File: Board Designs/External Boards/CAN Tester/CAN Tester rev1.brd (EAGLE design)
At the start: 160 x 100 mm, 25 parts, among them M1 Minifit, M2 Nanofit, U1 ISOLATED CAN TERMINAL, U2 TERMINATION_RESISTOR_JUMPER, U3 TEENSY_3.2_SIMPLE, U4 CHARACTER_LCD

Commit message: Moved the location of the can tester folder.
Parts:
- U1: value ISOLATED CAN TERMINAL -> ISOLATED CAN TRANSCIEVER
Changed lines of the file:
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@@
 <elements>
 <element name="U3" library="HyTechDevices" package="TEENSY_3.2_SIMPLE" value="TEENSY_3.2_SIMPLE" x="-19.05" y="1.27"/>
-<element name="U1" library="HyTechDevices" package="DUB8" value="ISOLATED CAN TERMINAL" x="-30.48" y="-30.48"/>
+<element name="U1" library="HyTechDevices" package="DUB8" value="ISOLATED CAN TRANSCIEVER" x="-30.48" y="-30.48"/>
 <element name="INCOMING" library="HyTechDevices" package="LED-805" value="YELLOW" x="-64.77" y="-72.39"/>
 <element name="OUTGOING" library="HyTechDevices" package="LED-805" value="BLUE" x="-71.12" y="-72.39"/>

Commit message: Verified schematic, but had to restart board
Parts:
- moved C2 306.9 mm to (-19.1, 116.8)
- moved C1 305.6 mm to (-15.2, 116.8)
- moved 5V_REGULATOR 282.7 mm to (-17.8, 110.5)
- moved CONTRAST_POT 257.5 mm to (-38.1, 81.3)
- moved R5 229.8 mm to (-38.1, 116.8)
- moved R4 228.3 mm to (-34.3, 116.8)
- moved R3 226.8 mm to (-30.5, 116.8)
- moved R2 225.4 mm to (-26.7, 116.8)
- moved R1 224.1 mm to (-22.9, 116.8)
- moved R_SPARE_BUTTON 219.9 mm to (-81.3, 108.0)
- moved R_MODE_SWITCH 217.2 mm to (-86.4, 108.0)
- moved M1 203.4 mm to (-63.5, 77.5)
- moved CAN_TERMINATION_RESISTOR 202.6 mm to (-74.9, 108.0)
- moved U4 200.9 mm to (-94.0, 39.4)
- moved U2 200.8 mm to (-67.3, 108.0)
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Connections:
- removed net N$15: R_MODE_SWITCH.2
- net GND: now also R_MODE_SWITCH.2

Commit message: Finished CAN_Tester Board
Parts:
- moved R_MODE_SWITCH 164.9 mm to (77.5, 88.9), turned to 270 degrees
- moved R_SPARE_BUTTON 160.8 mm to (77.5, 82.5), turned to 90 degrees
- moved CAN_TERMINATION_RESISTOR 153.8 mm to (67.3, 49.5), turned to 90 degrees
- moved INCOMING 153.6 mm to (72.4, 58.4), turned to 270 degrees
- moved U2 148.3 mm to (67.3, 45.7), turned to 90 degrees
- moved M1 147.3 mm to (64.8, 5.08)
- moved OUTGOING 146.7 mm to (72.4, 63.5), turned to 270 degrees
- moved SPARE 135.3 mm to (72.4, 78.7), turned to 270 degrees
- moved SPARE_BUTTON 124.5 mm to (71.1, 83.8)
- moved M2 123.4 mm to (48.3, 14.0)
- moved R5 113.3 mm to (68.6, 78.7), turned to 180 degrees
- moved MODE_SWITCH 113.0 mm to (71.1, 92.7)
- moved R4 111.6 mm to (68.6, 73.7), turned to 180 degrees
- moved ACKERR 111.3 mm to (72.4, 68.6), turned to 270 degrees
- moved R3 110.2 mm to (68.6, 68.6), turned to 180 degrees
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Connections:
- removed net VSS: U4.1
- net GND: now also U4.1
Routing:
- net GND: track 0.00 -> 309.8 mm
- net +5V: track 0.00 -> 139.2 mm
- net +3V3: track 0.00 -> 101.9 mm
- net CANL: track 0.00 -> 92.8 mm
- net +12V: track 0.00 -> 77.4 mm
- net CANH: track 0.00 -> 77.2 mm
- net CANTX: track 0.00 -> 42.6 mm
- net CANRX: track 0.00 -> 39.6 mm
- net N$22: track 0.00 -> 38.3 mm
- net N$20: track 0.00 -> 28.7 mm
- net VO: track 0.00 -> 27.4 mm
- net N$19: track 0.00 -> 26.8 mm
- net N$21: track 0.00 -> 26.3 mm
- net N$13: track 0.00 -> 17.5 mm
- net N$18: track 0.00 -> 17.4 mm
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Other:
- board size 160 x 100 mm -> 83.8 x 100.3 mm

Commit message: Actually finished CAN Tester board. Ready to be made for rev1
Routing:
- net GND: track 309.8 -> 326.9 mm
- net +12V: track 77.4 -> 79.2 mm

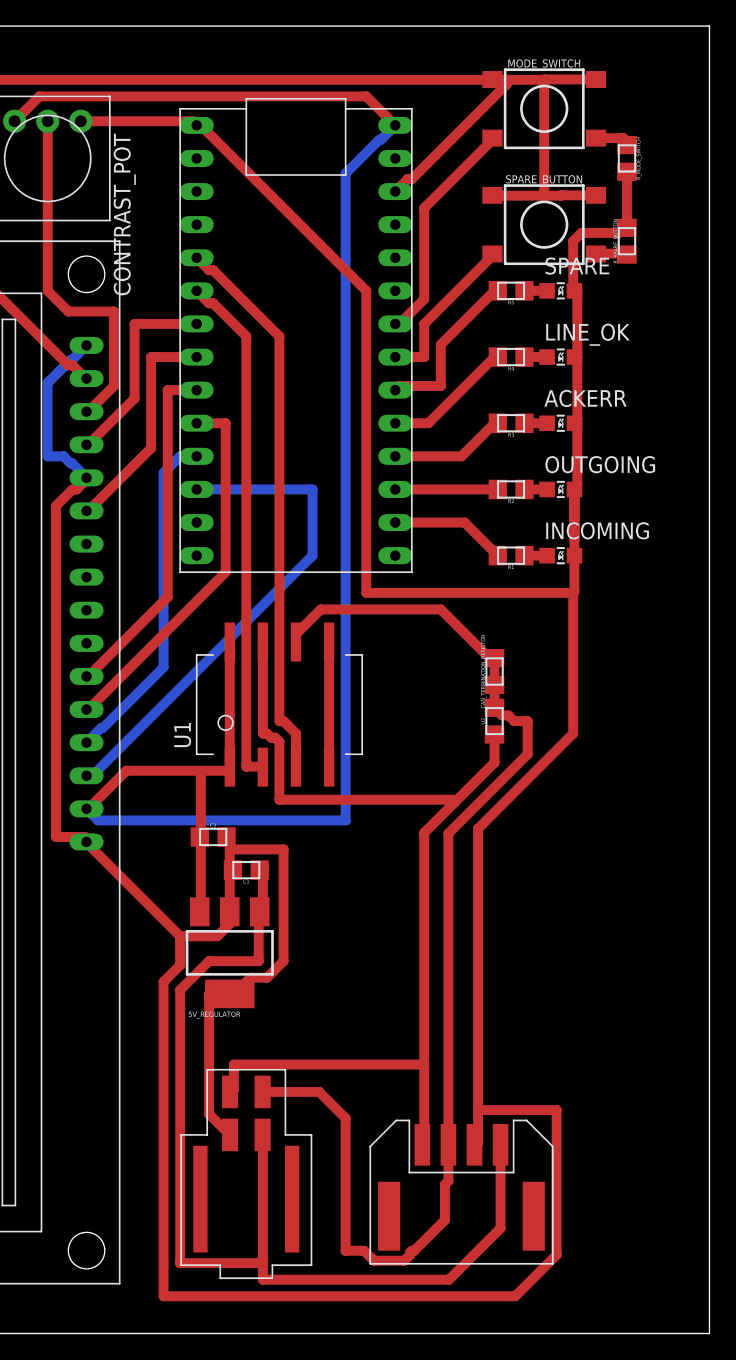
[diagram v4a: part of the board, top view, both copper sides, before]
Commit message: Added anothe rminifit and nano fit. Changed some components to through hole.
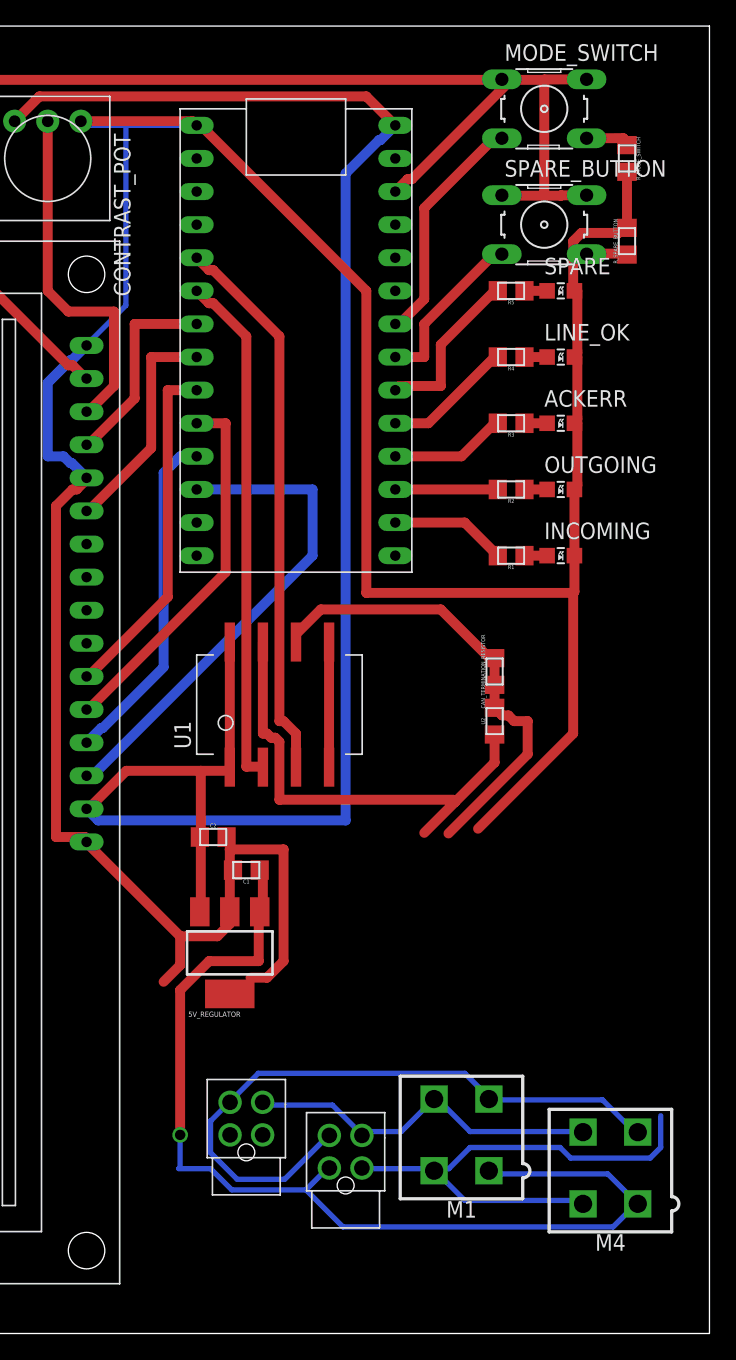
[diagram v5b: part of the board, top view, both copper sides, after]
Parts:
- added M3: Nanofit-1, HyTechDevices:NANO-FIT_VERTICAL-4
- added M4: Minifit-1, HyTechDevices:MINIFIT_5566-4
- M1: device HyTechDevices:DURACLIK_RIGHT_ANGLE-4 -> HyTechDevices:MINIFIT_5566-4
- M2: device HyTechDevices:NANO-FIT_RIGHT_ANGLE-4-SURFACE -> HyTechDevices:NANO-FIT_VERTICAL-4
- MODE_SWITCH, SPARE_BUTTON: device HyTechDevices:TACTILE_SWITCH_SMD_6.2MM_TALL -> HyTechDevices:B3F-10XX
- moved M1 8.89 mm to (64.8, 14.0)
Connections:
- net +12V: now also M2.P$1, M3.P$1, M4.1; no longer M2.1
- net +3V3: now also MODE_SWITCH.1, MODE_SWITCH.2, SPARE_BUTTON.1, SPARE_BUTTON.2; no longer MODE_SWITCH.B1, MODE_SWITCH.B2, SPARE_BUTTON.B1, SPARE_BUTTON.B2
- net CANH: now also M2.P$4, M3.P$4, M4.4; no longer M2.4
- net CANL: now also M2.P$3, M3.P$3, M4.3; no longer M2.3
- net GND: now also M2.P$2, M3.P$2, M4.2; no longer M2.2
- net N$12: now also MODE_SWITCH.4; no longer MODE_SWITCH.A2
- net N$13: now also MODE_SWITCH.3; no longer MODE_SWITCH.A1
- net N$14: now also SPARE_BUTTON.4; no longer SPARE_BUTTON.A2
- net N$3: now also SPARE_BUTTON.3; no longer SPARE_BUTTON.A1
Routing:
- net GND: track 326.9 -> 277.9 mm
- net CANH: track 77.2 -> 64.3 mm
- net CANL: track 92.6 -> 86.1 mm
- net +12V: track 79.2 -> 81.0 mm, vias 0 -> 1
- net N$14: track 2.46 -> 3.18 mm
- net N$12: track 2.74 -> 3.46 mm
- net N$3: track 12.3 -> 12.9 mm
- net N$13: track 17.5 -> 18.1 mm

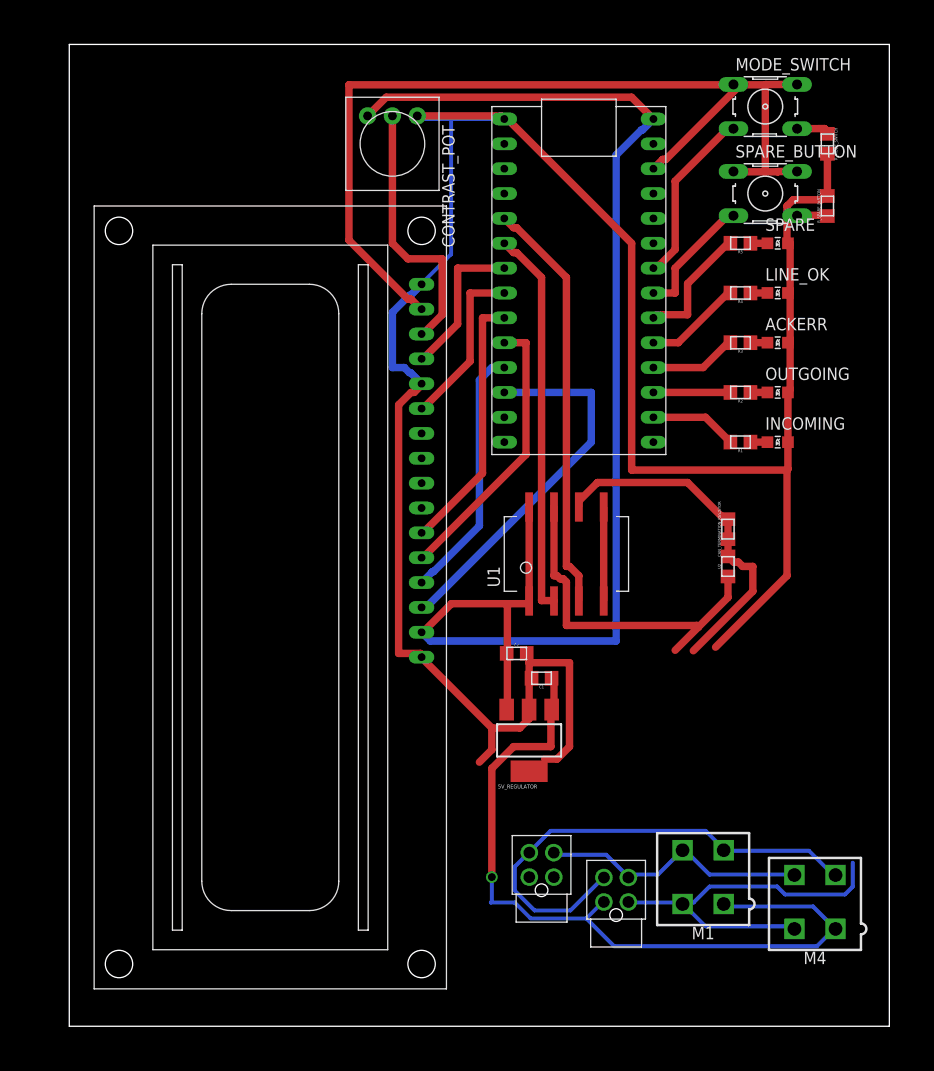
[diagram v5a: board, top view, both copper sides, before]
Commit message: Working on changes so the board can be made in the electronics lab
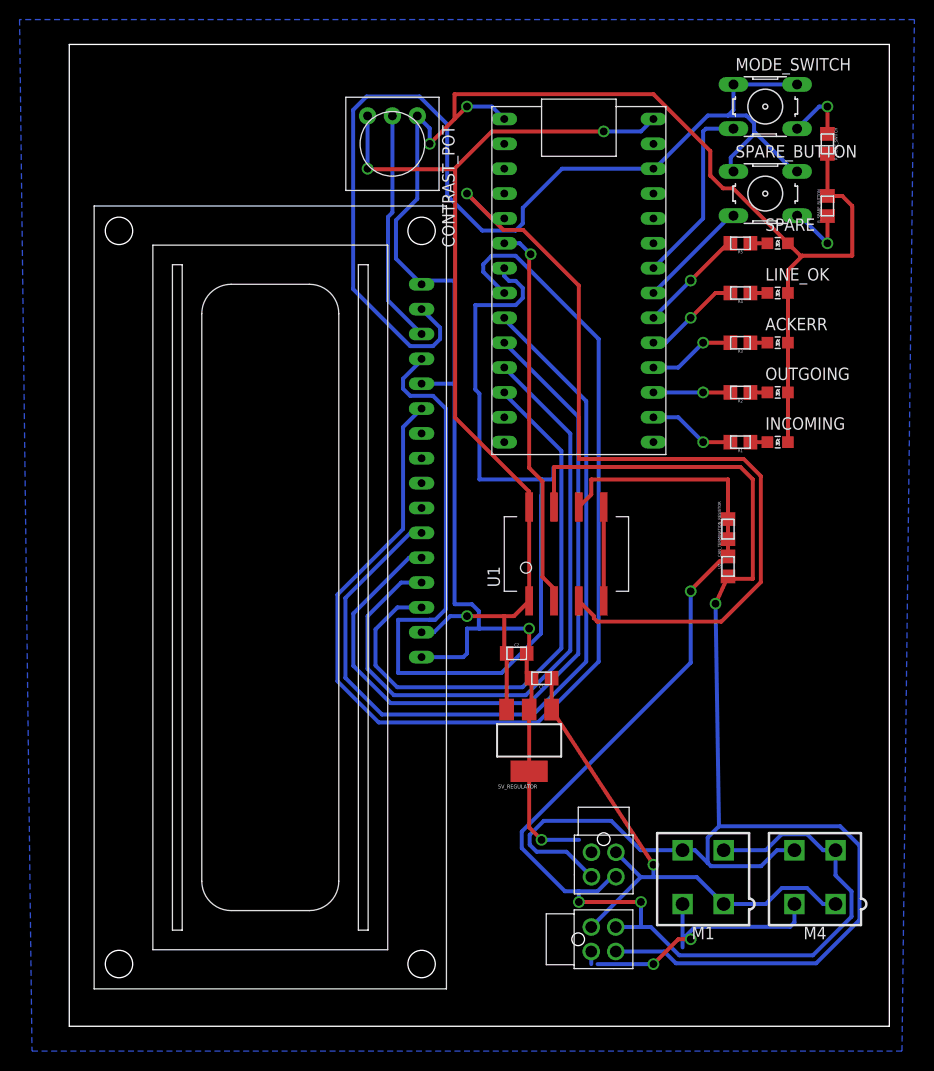
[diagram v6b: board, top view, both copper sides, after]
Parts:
- moved M2 8.13 mm to (53.3, 7.62), turned to 270 degrees
- moved M3 5.24 mm to (54.6, 16.5), turned to 180 degrees
- moved M4 2.54 mm to (76.2, 14.0)
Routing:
- net N$18: track 17.4 -> 114.9 mm
- net N$17: track 15.6 -> 108.9 mm
- net CANH: track 64.3 -> 156.7 mm, vias 0 -> 1
- net N$19: track 26.8 -> 85.7 mm
- net N$20: track 28.7 -> 76.3 mm
- net GND: track 277.9 -> 230.7 mm, vias 0 -> 6
- net CANL: track 86.1 -> 133.2 mm, vias 0 -> 3
- net CANTX: track 42.6 -> 89.3 mm, vias 0 -> 1
- net N$21: track 26.3 -> 67.8 mm
- net +5V: track 139.2 -> 106.1 mm, vias 0 -> 3
- net +12V: track 81.0 -> 56.6 mm
- net N$22: track 38.3 -> 60.6 mm
- net +3V3: track 102.1 -> 113.4 mm
- net N$14: track 3.18 -> 7.05 mm, vias 0 -> 1
- net VO: track 27.4 -> 23.9 mm
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- added copper zone on layer 16, net GND

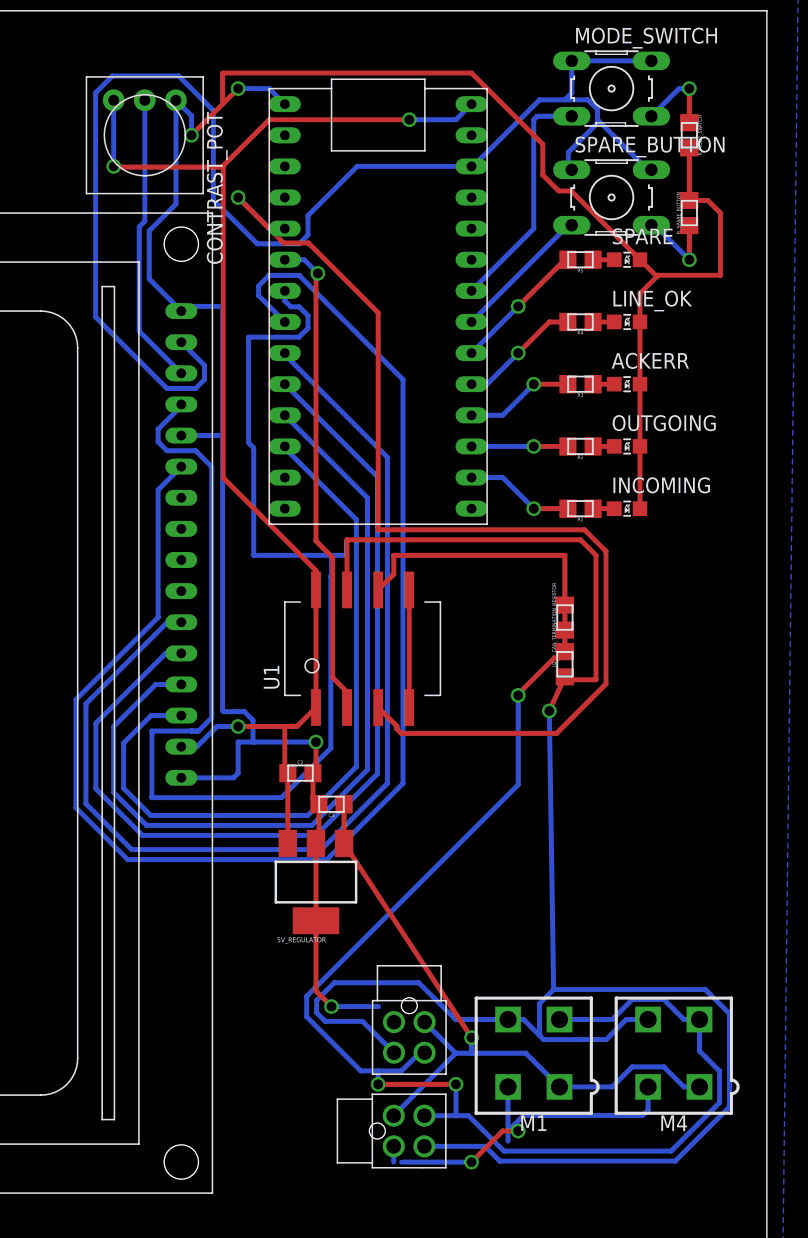
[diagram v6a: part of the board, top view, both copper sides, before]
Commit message: Almost done with CAN tester board, just changed the jumper package
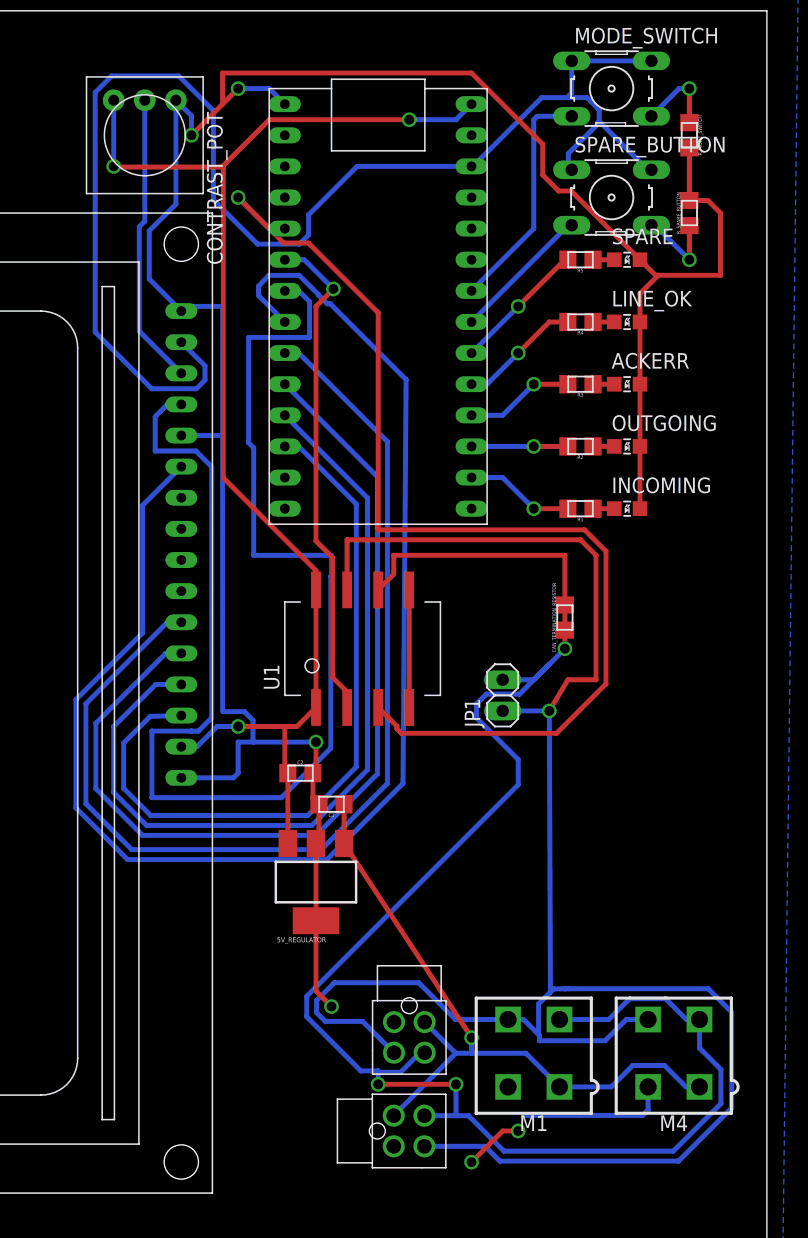
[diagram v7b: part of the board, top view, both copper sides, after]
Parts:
- removed U2: TERMINATION_RESISTOR_JUMPER, HyTechDevices:0805
- added JP1: M02, HyTechDevices:1X02
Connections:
- net CANH: now also JP1.1; no longer U2.1
- net CANL: now also JP1.2; no longer U2.2
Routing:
- net GND: track 230.7 -> 213.6 mm
- net CANL: track 133.2 -> 142.0 mm
- net CANH: track 156.7 -> 161.1 mm
- net CANRX: track 39.7 -> 40.8 mm
- net +3V3: track 113.4 -> 114.2 mm
- net N$19: track 85.7 -> 86.4 mm
- net N$17: track 108.9 -> 108.4 mm
